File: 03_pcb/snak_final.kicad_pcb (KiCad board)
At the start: 2 copper layers, 114 x 99.4 mm, 112 parts

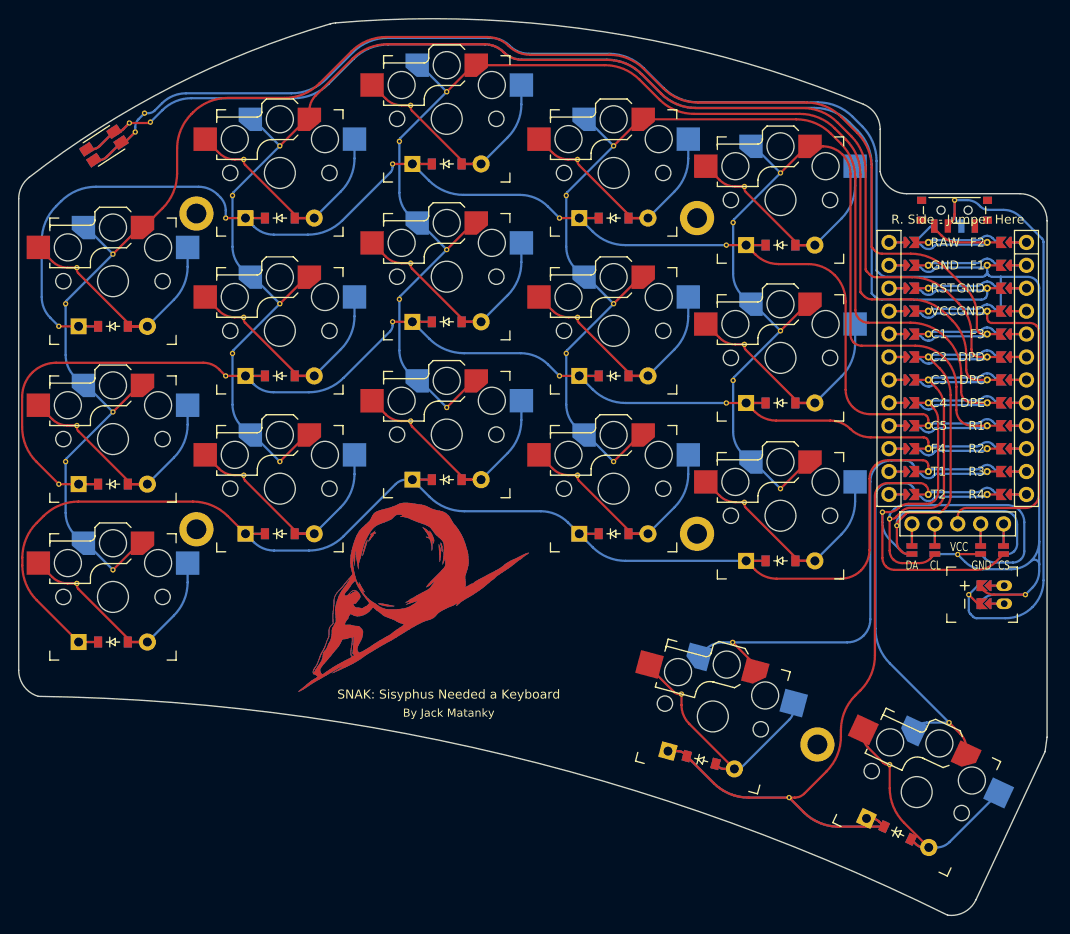
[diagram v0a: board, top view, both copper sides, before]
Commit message: update repo structure
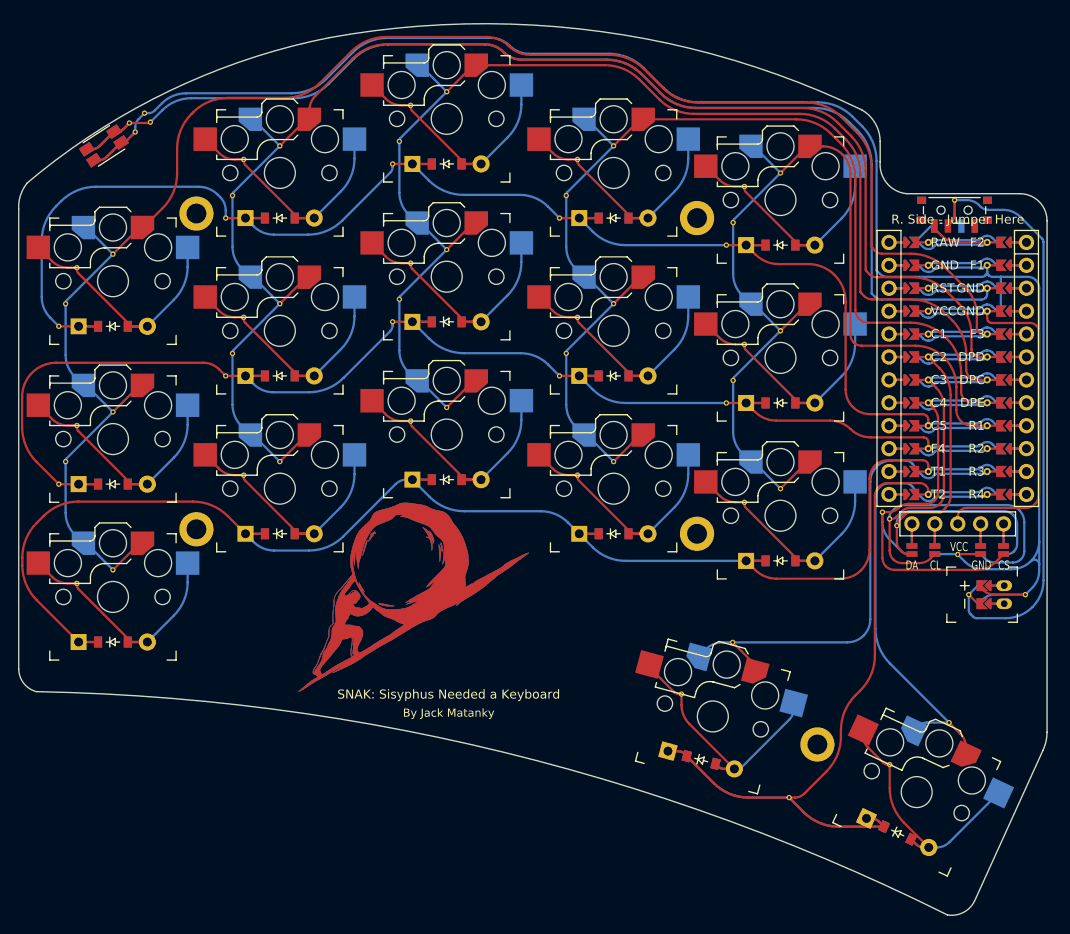
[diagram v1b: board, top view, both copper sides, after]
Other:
- board size 114 x 99.4 mm -> 114 x 98.8 mm
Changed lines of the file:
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@@
       (outputformat 1)
       (mirror false)
-      (drillshape 1)
+      (drillshape 0)
       (scaleselection 1)
-      (outputdirectory "")
+      (outputdirectory "_gerber/_snak_final/")
     )
   )
@@
   (gr_circle (center 109.25 57.5) (end 110.75 57.5)
     (stroke (width 0.15) (type solid)) (fill none) (layer "Eco2.User"))
-  (gr_line (start 203.55 58.3) (end 203.55 115.55)
+  (gr_line (start 203.55 58.3) (end 203.55 115)
     (stroke (width 0.15) (type solid)) (layer "Edge.Cuts"))
-  (gr_line (start 203.55 115.55) (end 203.329255 117.148209)
+  (gr_arc (start 91.5 110.5) (mid 143.38191 117.23569) (end 192.5 135.25)
     (stroke (width 0.15) (type solid)) (layer "Edge.Cuts"))
-  (gr_arc (start 91.729528 111.022192) (mid 143.483319 117.522792) (end 192.528304 135.279541)
+  (gr_arc (start 200.55 55.3) (mid 202.671321 56.178679) (end 203.55 58.3)
     (stroke (width 0.15) (type solid)) (layer "Edge.Cuts"))
-  (gr_arc (start 200.55 55.3) (mid 202.67132 56.17868) (end 203.55 58.3)
+  (gr_arc (start 124 38) (mid 154.133538 37.327659) (end 183 46)
     (stroke (width 0.15) (type solid)) (layer "Edge.Cuts"))
-  (gr_arc (start 124.094477 36.472495) (mid 124.381214 36.404248) (end 124.673265 36.364467)
+  (gr_line (start 203.1 117) (end 195.5 133.75)
     (stroke (width 0.15) (type solid)) (layer "Edge.Cuts"))
-  (gr_arc (start 124.673264 36.364467) (mid 154.476426 37.3582) (end 183.196172 45.382674)
+  (gr_arc (start 90.5 54.1) (mid 106.225911 43.919131) (end 124 38)
     (stroke (width 0.15) (type solid)) (layer "Edge.Cuts"))
-  (gr_line (start 203.329255 117.148209) (end 195.668338 133.577098)
+  (gr_arc (start 89.55 57) (mid 89.749709 55.459818) (end 90.5 54.1)
     (stroke (width 0.15) (type solid)) (layer "Edge.Cuts"))
-  (gr_arc (start 90.711341 53.482912) (mid 106.599129 43.400276) (end 124.094477 36.472495)
+  (gr_arc (start 188 55.3) (mid 185.789771 54.135965) (end 185.05 51.75)
     (stroke (width 0.15) (type solid)) (layer "Edge.Cuts"))
-  (gr_arc (start 89.55 55.853425) (mid 89.855934 54.533573) (end 90.71134 53.482912)
+  (gr_line (start 89.55 108) (end 89.55 57)
     (stroke (width 0.15) (type solid)) (layer "Edge.Cuts"))
-  (gr_arc (start 188 55.3) (mid 186.081186 54.606112) (end 185.05 52.845436)
-    (stroke (width 0.15) (type solid)) (layer "Edge.Cuts"))
-  (gr_line (start 89.55 108.136568) (end 89.55 55.853425)
-    (stroke (width 0.15) (type solid)) (layer "Edge.Cuts"))
-  (gr_arc (start 91.729527 111.022192) (mid 90.15611 109.944686) (end 89.55 108.136568)
+  (gr_arc (start 203.55 115) (mid 203.434518 116.024642) (end 203.1 117)
+    (stroke (width 0.15) (type default)) (layer "Edge.Cuts"))
+  (gr_arc (start 91.5 110.5) (mid 90.105981 109.576835) (end 89.55 108)
     (stroke (width 0.15) (type solid)) (layer "Edge.Cuts"))
   (gr_line (start 188 55.3) (end 200.55 55.3)
     (stroke (width 0.15) (type solid)) (layer "Edge.Cuts"))
-  (gr_line (start 185.05 52.845436) (end 185.05 48.15509)
+  (gr_line (start 185.05 51.75) (end 185.05 49.5)
     (stroke (width 0.15) (type solid)) (layer "Edge.Cuts"))
-  (gr_arc (start 195.668337 133.577097) (mid 194.379297 134.946558) (end 192.528304 135.27954)
+  (gr_arc (start 195.5 133.75) (mid 194.247565 134.995129) (end 192.5 135.25)
     (stroke (width 0.15) (type solid)) (layer "Edge.Cuts"))
-  (gr_arc (start 183.196172 45.382674) (mid 184.543844 46.487534) (end 185.05 48.15509)
+  (gr_arc (start 183 46) (mid 184.493911 47.475352) (end 185.05 49.5)
     (stroke (width 0.15) (type solid)) (layer "Edge.Cuts"))
   (segment (start 195.77 70.160086) (end 195.77 68.73) (width 0.25) (layer "F.Cu") (net 1))

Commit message: update before moving files
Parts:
- moved REF** 4.82 mm to (142.0, 112.5)
- moved G*** 2.63 mm to (135.1, 100.4)
